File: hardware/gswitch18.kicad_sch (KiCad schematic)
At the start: 26 parts, among them P1 CONN_6X2, P2 CONN_6X2, P3 CONN_6X2, P4 USB, P5 ISP, U1 ATMEGA88P, X1 12MHz

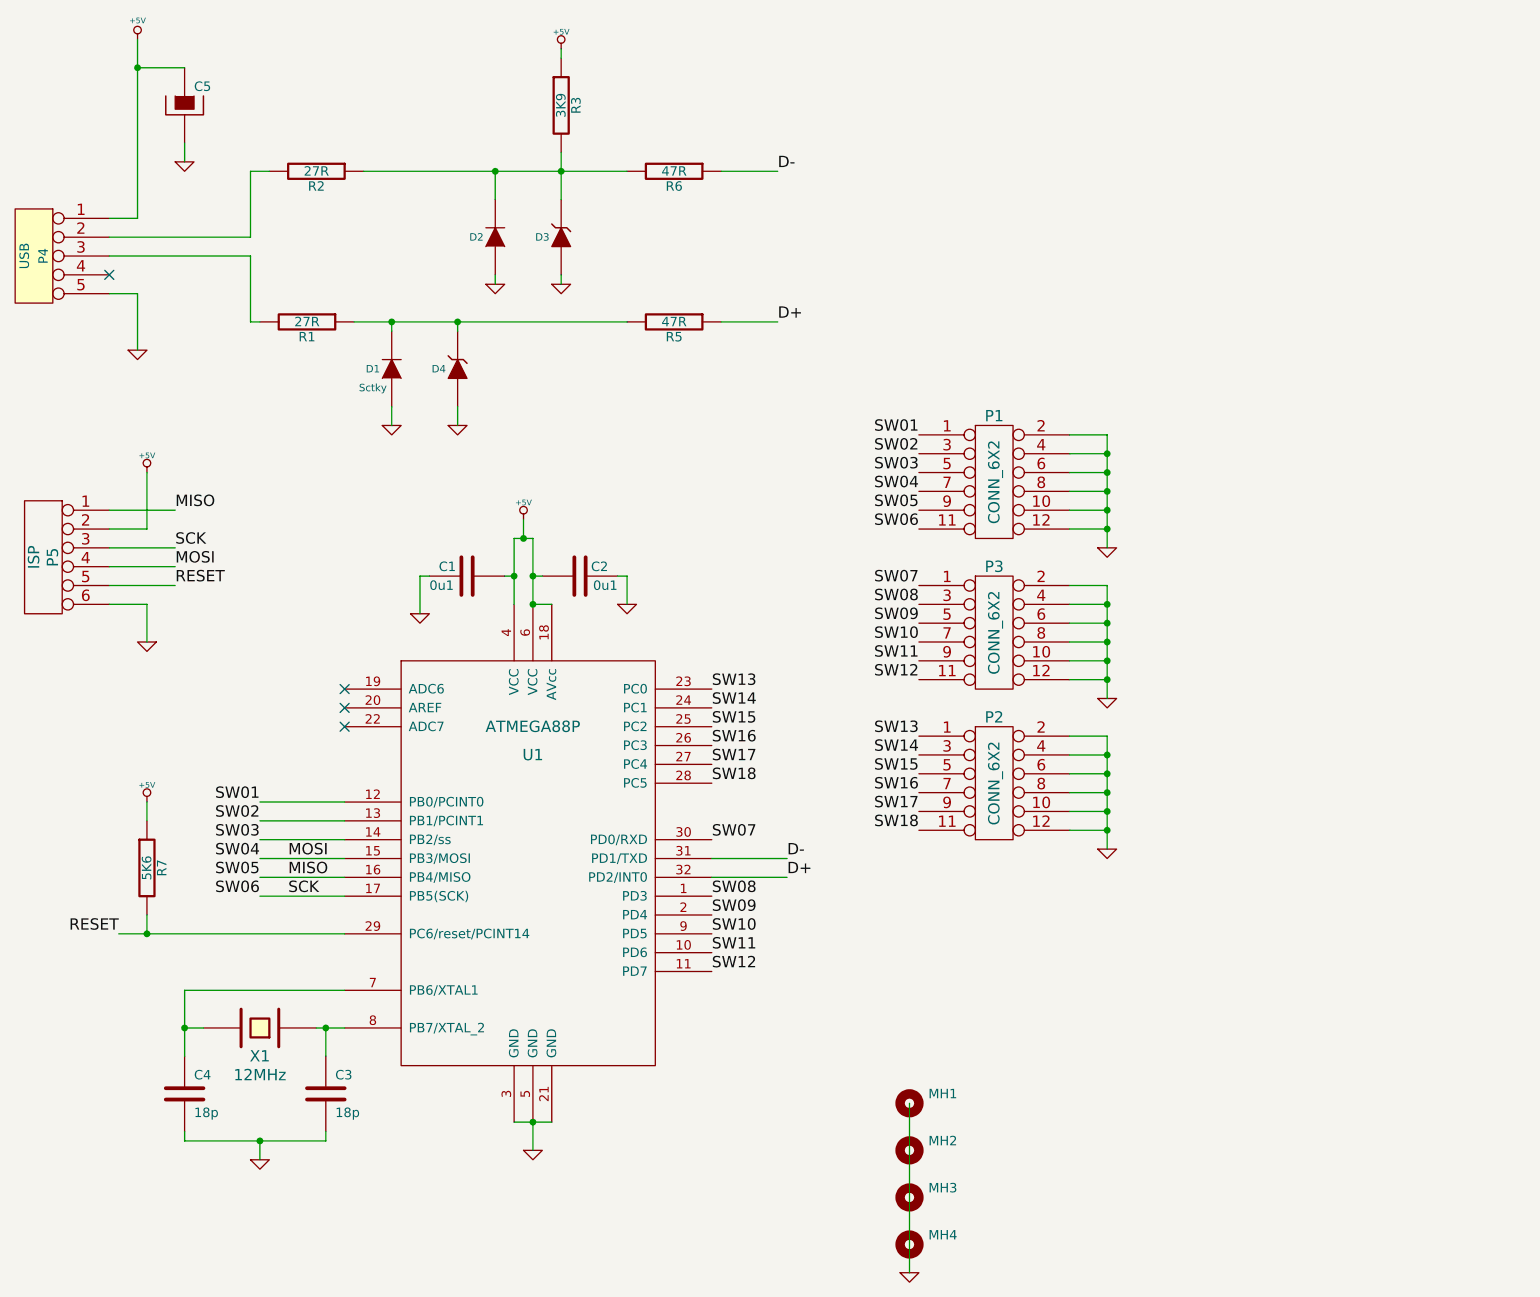
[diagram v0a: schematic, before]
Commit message: Updated to KiCAD v6. Bumped versionto v1.2 TH (through-hole). DEPRECATED; See smd branch.
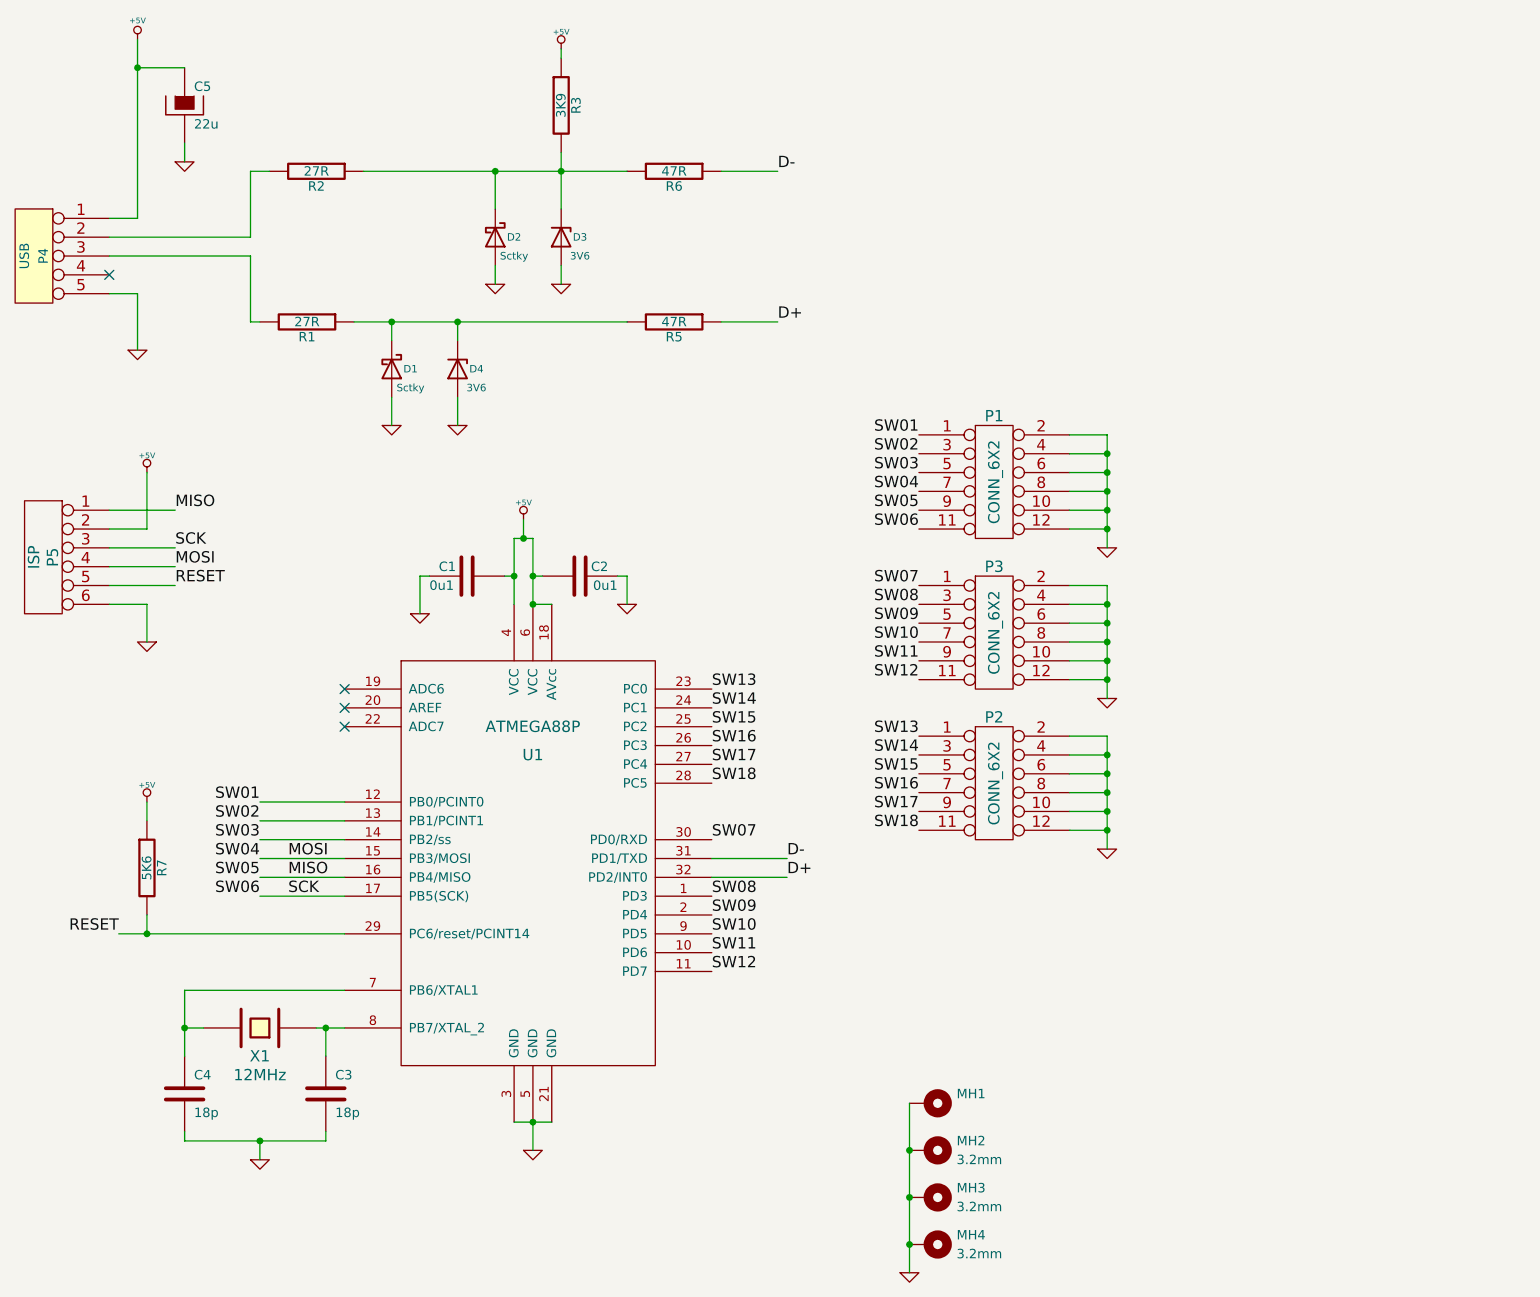
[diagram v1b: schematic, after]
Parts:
- C5: value (none) -> 22u; footprint (none) -> Capacitor_Tantalum_SMD:CP_EIA-3216-18_Kemet-A
- D1: symbol gswitch18-rescue:DIODE -> Device:D_Schottky
- D2: value (none) -> Sctky; footprint (none) -> Diode_SMD:D_SOD-523; symbol gswitch18-rescue:DIODE -> Device:D_Schottky
- D3, D4: value (none) -> 3V6; footprint Capacitor_SMD:C_1206_3216Metric_Pad1.33x1.80mm_HandSolder -> Diode_SMD:D_MiniMELF; symbol gswitch18-rescue:ZENER -> Device:D_Zener
- MH2, MH3, MH4: value (none) -> 3.2mm; footprint (none) -> MountingHole:MountingHole_3.2mm_M3_Pad_Via
- P1, P2, P3: footprint pin_array_6x2 -> Connector_PinHeader_2.54mm:PinHeader_2x06_P2.54mm_Vertical
- P4: footprint USB-B_mini -> Connector_USB:USB_Mini-B_Lumberg_2486_01_Horizontal
- X1: footprint HC-49V -> Crystal:Crystal_HC49-4H_Vertical
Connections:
- net GND: now also D3.2 (A), D4.2 (A), MH1.1 (GND), MH2.1 (GND), MH3.1 (GND), MH4.1 (GND); no longer D3.1 (A), D4.1 (A)
- net at D2.1 (K), R2.1, R3.2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: now also D3.1 (K); no longer D3.2 (K)
- net at D1.1 (K), R1.1, R5.2: now also D4.1 (K); no longer D4.2 (K)
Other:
- company: (none) -> https://github.com/gruvin/gswitch18
- title: G9X USB Programmer -> 18 Button USB Game Controller
- moved on the sheet: D1, D2, D3, D4

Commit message: updated to KiCAD 7.0
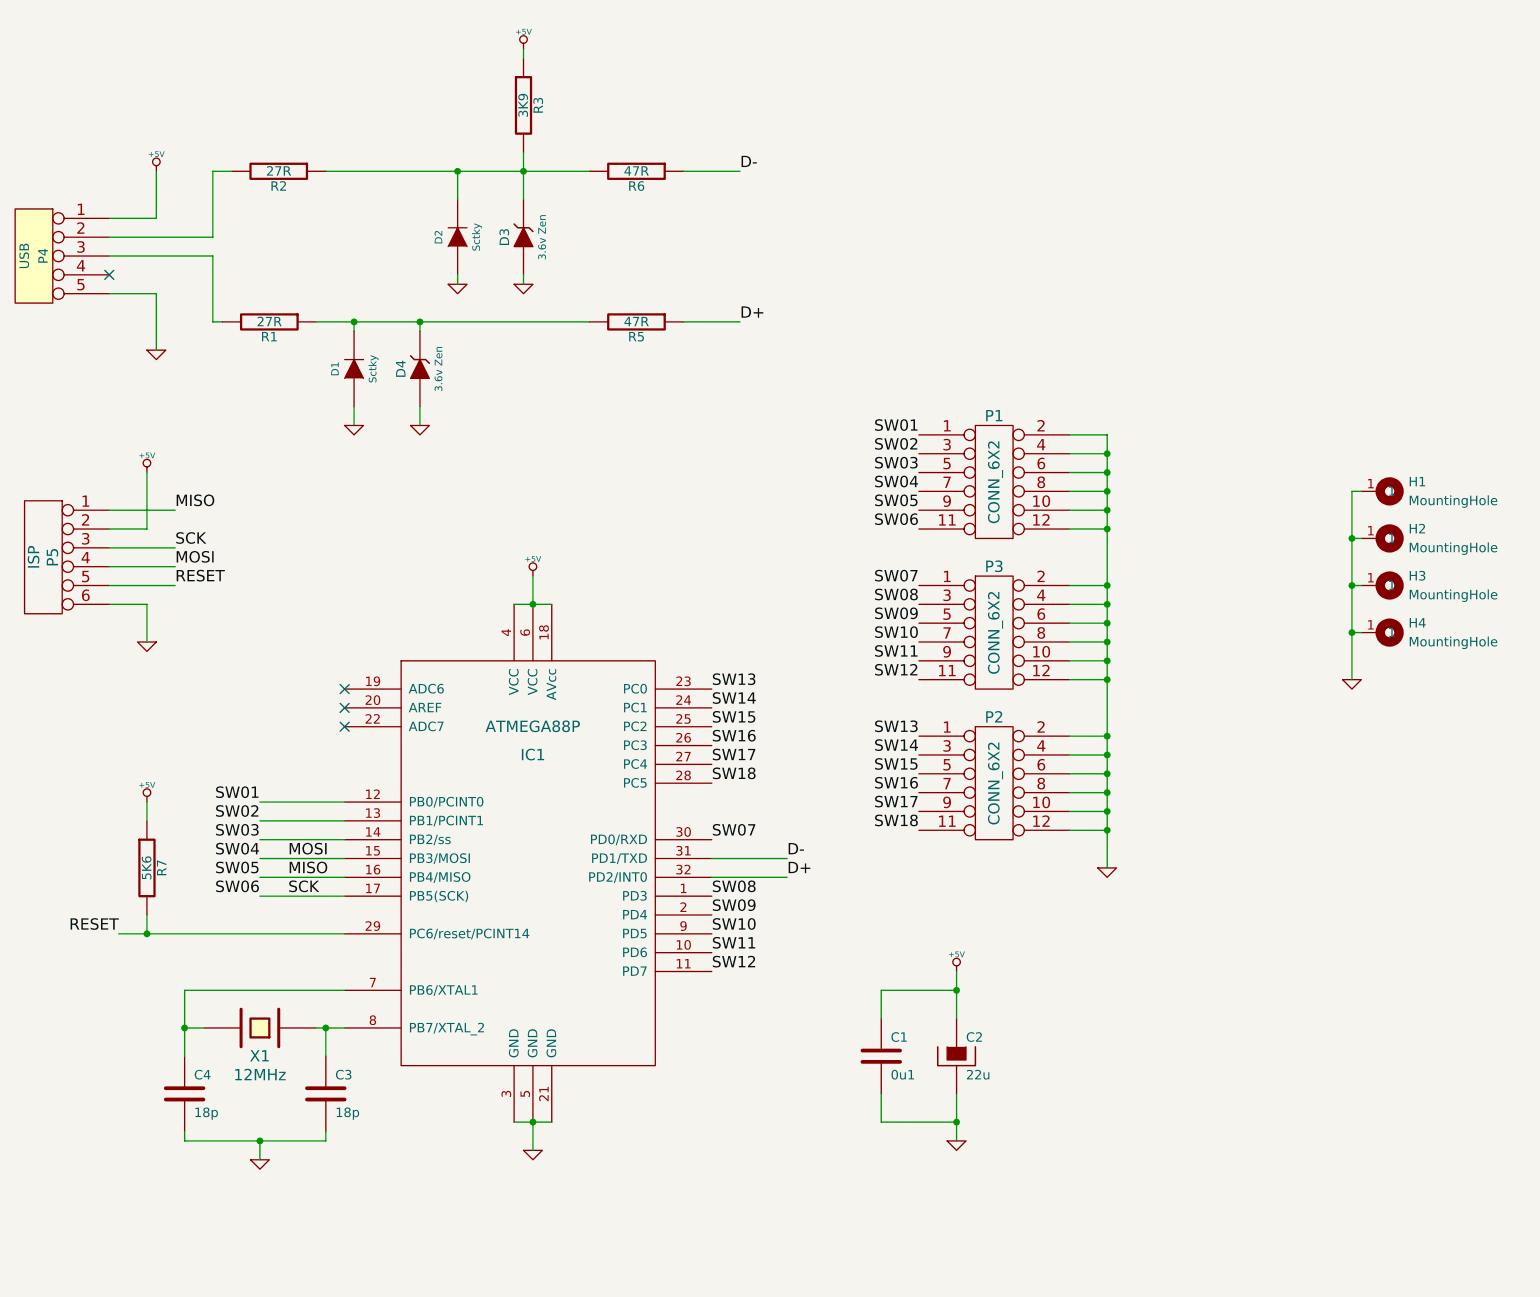
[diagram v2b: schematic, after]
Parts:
- removed C1: 0u1, Capacitor_SMD:C_0603_1608Metric, symbol gswitch18-rescue:C
- removed C5: 22u, Capacitor_Tantalum_SMD:CP_EIA-3216-18_Kemet-A, symbol gswitch18-rescue:CAPAPOL
- removed MH1: (no value), symbol Mechanical:MountingHole
- removed MH2, MH3, MH4: 3.2mm, MountingHole:MountingHole_3.2mm_M3_Pad_Via, symbol Mechanical:MountingHole
- added C2: 22u, Capacitor_Tantalum_SMD:CP_EIA-3528-21_Kemet-B, symbol gswitch18-rescue:CAPAPOL
- added H1, H2, H3, H4: MountingHole, MountingHole:MountingHole_3.2mm_M3_Pad_Via, symbol Mechanical:MountingHole
- D1, D2: symbol Device:D_Schottky -> gswitch18-rescue:DIODE
- D3, D4: value 3V6 -> 3.6v Zen; symbol Device:D_Zener -> gswitch18-rescue:ZENER
- IC1: renamed from U1; symbol atmega48p:ATMEGA48P -> gswitch18-rescue:ATMEGA48P
- P4: footprint Connector_USB:USB_Mini-B_Lumberg_2486_01_Horizontal -> Connector_USB:USB_Mini-B_Wuerth_65100516121_Horizontal
- P5: footprint pin_array_3x2 -> Connector_PinHeader_2.54mm:PinHeader_2x03_P2.54mm_Vertical
- R1, R2, R3, R5, R6, R7: footprint Resistor_SMD:R_0603_1608Metric -> Resistor_SMD:R_0603_1608Metric_Pad0.98x0.95mm_HandSolder
- renumbered C2 to C1
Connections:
- net +5V: now also C2.1
- net GND: now also D1.1 (A), D2.1 (A), D3.1 (A), D4.1 (A), C2.2, H1.1, H2.1, H3.1, H4.1; no longer D1.2 (A), D2.2 (A), D3.2 (A), D4.2 (A)
- net at R2.1, R3.2, R6.2: now also D2.2 (K), D3.2 (K); no longer D2.1 (K), D3.1 (K)
- net at R1.1, R5.2: now also D1.2 (K), D4.2 (K); no longer D1.1 (K), D4.1 (K)
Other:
- company: https://github.com/gruvin/gswitch18 -> (none)
- title: 18 Button USB Game Controller -> G9X USB Programmer
- moved on the sheet: C1, D1, D2, D3, D4, R1, R2, R3, R5, R6
